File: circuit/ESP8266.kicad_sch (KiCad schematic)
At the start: 39 parts, among them J1 Conn_02x04_Odd_Even, K1 SW_DIP_x01, K2 SW_DIP_x01, P1 USB_C_Plug_USB2.0, U1 W25Q64, U2 ESP8266EX, U3 HX9193, U4 CH330N, Y1 26MHz

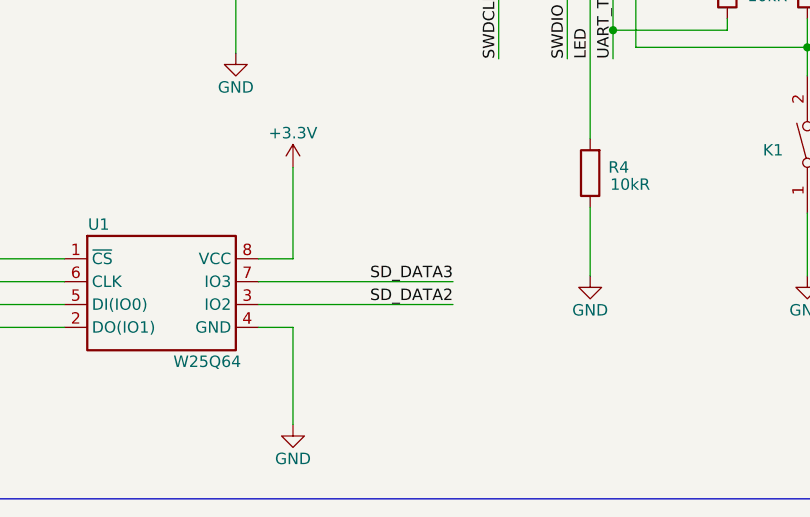
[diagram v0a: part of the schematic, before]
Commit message: Update circuit, fix issue #29  (#30)
* Update circuit, Fix issue #29

* Update README_CN, Translate from README.
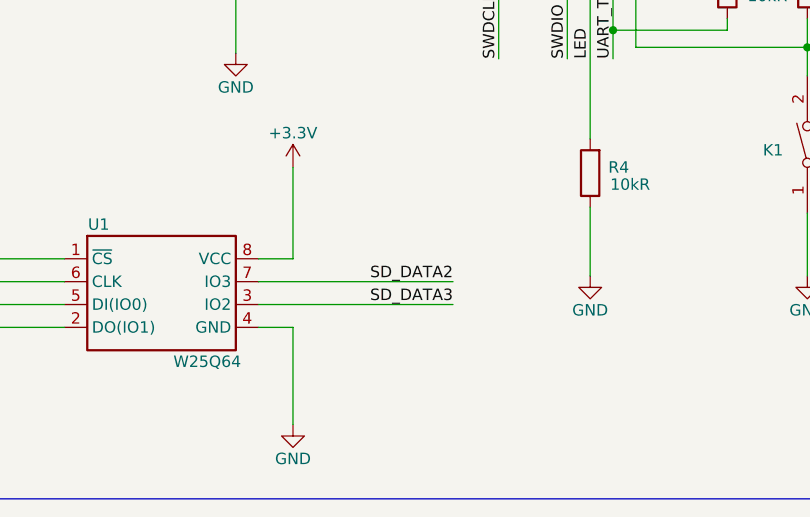
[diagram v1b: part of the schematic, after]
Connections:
- net SD_DATA2: now also U1.7 (IO3); no longer U1.3 (IO2)
- net SD_DATA3: now also U1.3 (IO2); no longer U1.7 (IO3)
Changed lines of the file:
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@@
   (title_block
     (title "ESP8266 Wireless DAP")
-    (date "2022-02-02")
-    (rev "Version 1.2.1")
+    (date "2022-02-19")
+    (rev "Version 1.2.2")
   )
   (junction (at 121.92 127.635) (diameter 0) (color 0 0 0 0)
@@
     (effects (font (size 1.27 1.27)) (justify right bottom))
   )
-  (label "SD_DATA2" (at 91.44 172.72 180)
-    (effects (font (size 1.27 1.27)) (justify right bottom))
-  )
-  (label "SD_DATA3" (at 91.44 170.18 180)
-    (effects (font (size 1.27 1.27)) (justify right bottom))
-  )
+  (label "SD_DATA2" (at 91.44 170.18 180)
+    (effects (font (size 1.27 1.27)) (justify right bottom))
+  )
+  (label "SD_DATA3" (at 91.44 172.72 180)
+    (effects (font (size 1.27 1.27)) (justify right bottom))
+  )
